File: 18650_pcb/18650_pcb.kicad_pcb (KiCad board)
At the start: 2 copper layers, 40 x 88 mm, 3 parts, among them P1 CONN_01X02

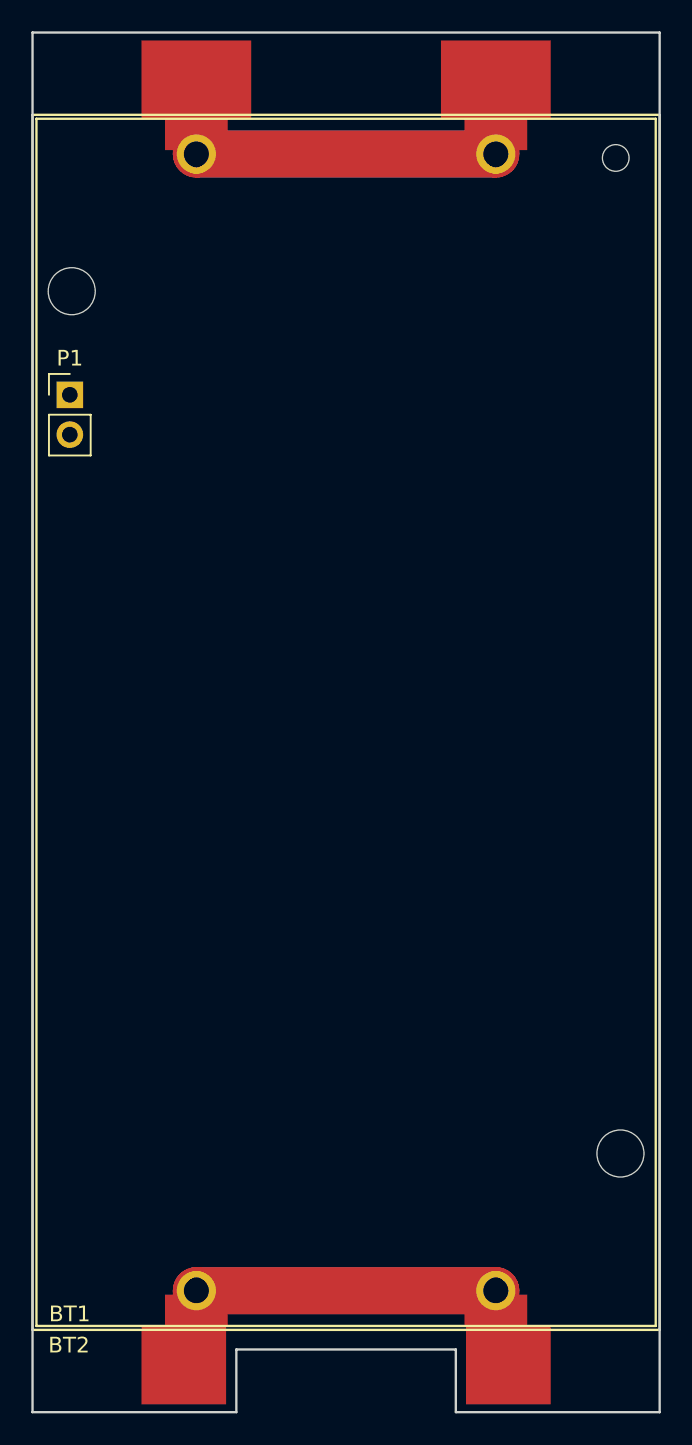
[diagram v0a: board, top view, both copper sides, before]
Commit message: Almost ready; needs cutouts for breakouts and positioning of connector
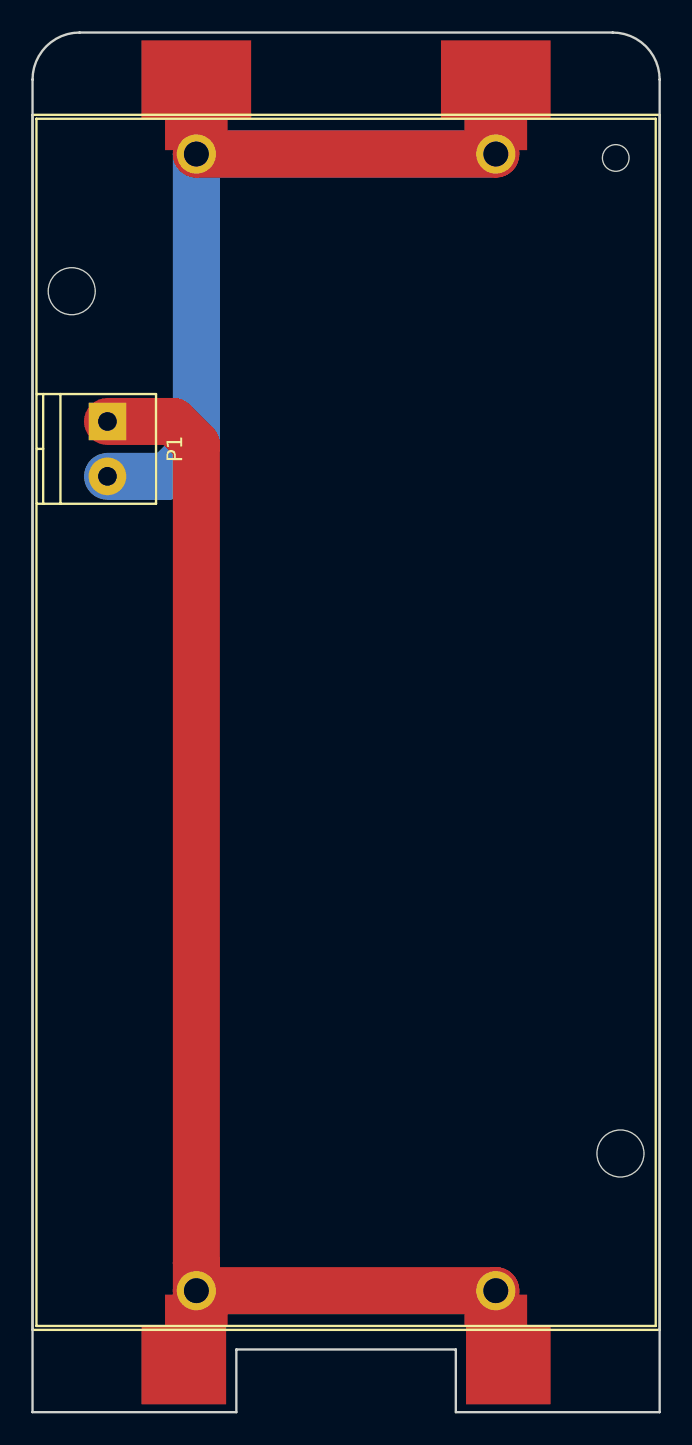
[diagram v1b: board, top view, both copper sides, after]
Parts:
- BT1: footprint footprints:KEYSTONE_1048_1049 -> footprints:KEYSTONE_1048
- P1: footprint Pin_Headers:Pin_Header_Straight_1x02_Pitch2.54mm -> Terminal_Blocks:TerminalBlock_Pheonix_PT-3.5mm_2pol
- moved P1 2.94 mm to (134.8, 80.8), turned to 270 degrees
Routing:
- net Net-(BT1-Pad3): track 47.7 -> 108.0 mm
- net Net-(BT1-Pad1): track 47.7 -> 72.8 mm
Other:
- outline, holes or cut-outs redrawn

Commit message: Finished 18650 PCB
* Added LED cutout
* Added battery charge module cutout
* Checked dimensions
* Added DC-DC cutout
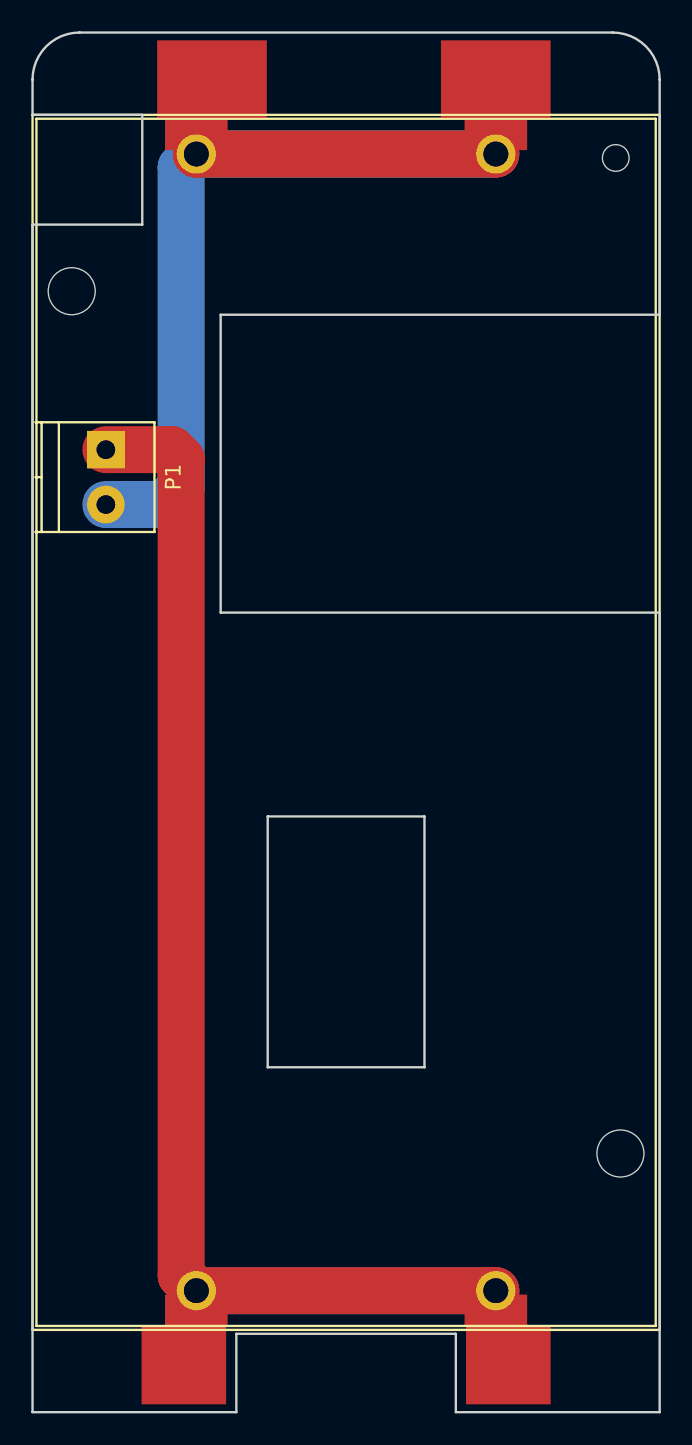
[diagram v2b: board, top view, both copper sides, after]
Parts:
- moved P1 1.80 mm to (134.7, 82.6)
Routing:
- net Net-(BT1-Pad1): track 72.8 -> 74.7 mm
- net Net-(BT1-Pad3): track 108.0 -> 106.2 mm
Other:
- outline, holes or cut-outs redrawn
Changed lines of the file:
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@@
     (area 129.924999 55.924999 170.075001 144.075001)
     (thickness 1.6)
-    (drawings 10)
-    (tracks 15)
+    (drawings 22)
+    (tracks 17)
     (zones 0)
     (modules 3)
@@
   )
   (setup
-    (last_trace_width 0.25)
+    (last_trace_width 3)
     (user_trace_width 3)
     (trace_clearance 0.2)
@@
     (mod_text_size 1 1)
     (mod_text_width 0.15)
-    (pad_size 5.4 5)
+    (pad_size 7 5)
     (pad_drill 0)
     (pad_to_mask_clearance 0.2)
@@
     (visible_elements 7FFFFFFF)
     (pcbplotparams
-      (layerselection 0x00030_80000001)
-      (usegerberextensions false)
+      (layerselection 0x010f0_80000001)
+      (usegerberextensions true)
+      (usegerberattributes true)
       (excludeedgelayer true)
       (linewidth 0.200000)
@@
       (psnegative false)
       (psa4output false)
-      (plotreference true)
-      (plotvalue true)
+      (plotreference false)
+      (plotvalue false)
       (plotinvisibletext false)
       (padsonsilk false)
@@
       (outputformat 1)
       (mirror false)
-      (drillshape 1)
+      (drillshape 0)
       (scaleselection 1)
-      (outputdirectory ""))
+      (outputdirectory gerbers/))
   )
   (net 0 "")
@@
       (effects (font (size 1 1) (thickness 0.15)))
     )
-    (fp_text value 2x_Battery_Holder (at 18.57862 -26.69196 90) (layer B.Fab)
+    (fp_text value 2x_Battery_Holder (at -0.12138 -27.49196) (layer B.Fab)
       (effects (font (size 1 1) (thickness 0.15)) (justify mirror))
     )
@@
       (effects (font (size 1 1) (thickness 0.15)))
     )
-    (fp_text value 2x_Battery_Holder (at 18.57862 -26.89196 90) (layer F.Fab)
+    (fp_text value 2x_Battery_Holder (at 0.37862 -29.59196 180) (layer F.Fab)
       (effects (font (size 1 1) (thickness 0.15)))
     )
@@
     (fp_line (start 19.75 -38.5) (end 19.75 38.5) (layer F.SilkS) (width 0.15))
     (fp_line (start -19.75 -38.5) (end 19.75 -38.5) (layer F.SilkS) (width 0.15))
-    (pad 1 smd rect (at -9.55 -41) (size 7 5) (layers F.Cu F.Paste F.Mask)
+    (pad 1 smd rect (at -8.55 -41) (size 7 5) (layers F.Cu F.Paste F.Mask)
       (net 1 "Net-(BT1-Pad1)"))
     (pad 2 smd rect (at 9.55 -41) (size 7 5) (layers F.Cu F.Paste F.Mask)
@@
   )
   (module Terminal_Blocks:TerminalBlock_Pheonix_PT-3.5mm_2pol (layer F.Cu)
-    (at 134.77862 80.80804 270)
+    (at 134.67862 82.60804 270)
     (descr "2-way 3.5mm pitch terminal block, Phoenix PT series")
     (fp_text reference P1 (at 1.75 -4.3 270) (layer F.SilkS)
@@
     )
   )
+  (gr_line (start 137 61.25) (end 130 61.25) (layer Edge.Cuts) (width 0.15))
+  (gr_line (start 137 61.25) (end 137 68.25) (layer Edge.Cuts) (width 0.15))
+  (gr_line (start 130 68.25) (end 137 68.25) (layer Edge.Cuts) (width 0.15))
+  (gr_line (start 130 144) (end 130 68.25) (layer Edge.Cuts) (width 0.15))
+  (gr_line (start 145 106) (end 145 122) (layer Edge.Cuts) (width 0.15))
+  (gr_line (start 145 122) (end 155 122) (layer Edge.Cuts) (width 0.15))
+  (gr_line (start 155 106) (end 155 122) (layer Edge.Cuts) (width 0.15))
+  (gr_line (start 145 106) (end 155 106) (layer Edge.Cuts) (width 0.15))
+  (gr_line (start 170 144) (end 170 93) (layer Edge.Cuts) (width 0.15))
+  (gr_line (start 142 93) (end 170 93) (layer Edge.Cuts) (width 0.15))
+  (gr_line (start 142 74) (end 142 93) (layer Edge.Cuts) (width 0.15))
+  (gr_line (start 142 74) (end 170 74) (layer Edge.Cuts) (width 0.15))
   (gr_arc (start 133 59) (end 130 59) (angle 90) (layer Edge.Cuts) (width 0.15))
   (gr_arc (start 167 59) (end 167 56) (angle 90) (layer Edge.Cuts) (width 0.15))
-  (gr_line (start 130 144) (end 130 59) (layer Edge.Cuts) (width 0.15))
+  (gr_line (start 130 61.25) (end 130 59) (layer Edge.Cuts) (width 0.15))
   (gr_line (start 143 144) (end 130 144) (layer Edge.Cuts) (width 0.15))
-  (gr_line (start 143 140) (end 143 144) (layer Edge.Cuts) (width 0.15))
-  (gr_line (start 143 140) (end 157 140) (layer Edge.Cuts) (width 0.15))
-  (gr_line (start 157 140) (end 157 144) (layer Edge.Cuts) (width 0.15))
+  (gr_line (start 143 139) (end 143 144) (layer Edge.Cuts) (width 0.15))
+  (gr_line (start 143 139) (end 157 139) (layer Edge.Cuts) (width 0.15))
+  (gr_line (start 157 139) (end 157 144) (layer Edge.Cuts) (width 0.15))
   (gr_line (start 170 144) (end 157 144) (layer Edge.Cuts) (width 0.15))
-  (gr_line (start 170 144) (end 170 59) (layer Edge.Cuts) (width 0.15))
+  (gr_line (start 170 74) (end 170 59) (layer Edge.Cuts) (width 0.15))
   (gr_line (start 133 56) (end 167 56) (layer Edge.Cuts) (width 0.15))
-  (segment (start 138.57862 84.30804) (end 140.45 82.43666) (width 3) (layer B.Cu) (net 1))
-  (segment (start 134.77862 84.30804) (end 138.57862 84.30804) (width 3) (layer B.Cu) (net 1))
-  (segment (start 140.45 82.43666) (end 140.45 63.75) (width 3) (layer B.Cu) (net 1))
+  (segment (start 139.47862 85.00804) (end 139.47862 64.60804) (width 3) (layer B.Cu) (net 1))
+  (segment (start 134.67862 86.10804) (end 138.37862 86.10804) (width 3) (layer B.Cu) (net 1))
+  (segment (start 138.37862 86.10804) (end 139.47862 85.00804) (width 3) (layer B.Cu) (net 1))
+  (segment (start 139.47862 64.60804) (end 140.33666 63.75) (width 3) (layer B.Cu) (net 1))
+  (segment (start 140.33666 63.75) (end 140.45 63.75) (width 3) (layer B.Cu) (net 1))
   (segment (start 140.45 63.75) (end 159.55 63.75) (width 3) (layer F.Cu) (net 1))
   (segment (start 140.45 59) (end 140.45 63.75) (width 3) (layer F.Cu) (net 1))
   (segment (start 159.55 59) (end 159.55 63.75) (width 3) (layer F.Cu) (net 1))
   (segment (start 140.45 63.75) (end 159.55 63.75) (width 3) (layer B.Cu) (net 1))
-  (segment (start 134.77862 80.80804) (end 138.97862 80.80804) (width 3) (layer F.Cu) (net 2))
-  (segment (start 138.97862 80.80804) (end 140.45 82.27942) (width 3) (layer F.Cu) (net 2))
-  (segment (start 140.45 82.27942) (end 140.45 134.482234) (width 3) (layer F.Cu) (net 2))
-  (segment (start 140.45 134.482234) (end 140.45 136.25) (width 3) (layer F.Cu) (net 2))
+  (segment (start 134.67862 82.60804) (end 138.87862 82.60804) (width 3) (layer F.Cu) (net 2))
+  (segment (start 138.87862 82.60804) (end 139.47862 83.20804) (width 3) (layer F.Cu) (net 2))
+  (segment (start 139.47862 83.20804) (end 139.47862 135.27862) (width 3) (layer F.Cu) (net 2))
+  (segment (start 139.47862 135.27862) (end 140.45 136.25) (width 3) (layer F.Cu) (net 2))
   (segment (start 159.55 136.25) (end 140.45 136.25) (width 3) (layer B.Cu) (net 2))
   (segment (start 159.55 136.25) (end 159.55 141) (width 3) (layer F.Cu) (net 2))
